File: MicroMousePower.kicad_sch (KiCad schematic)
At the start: 40 parts, among them J1 USB_C_Receptacle_PowerOnly_6P, J2 Conn_02x16_Odd_Even, J3 Conn_01x02_Pin, T1 TIP31C, U1 INA219AxDCN, U2 MCP73831-3-MC, U3 CH224K, U4 DRV8833PW, U5 DRV8833PW, U6 TPS61023DRLR

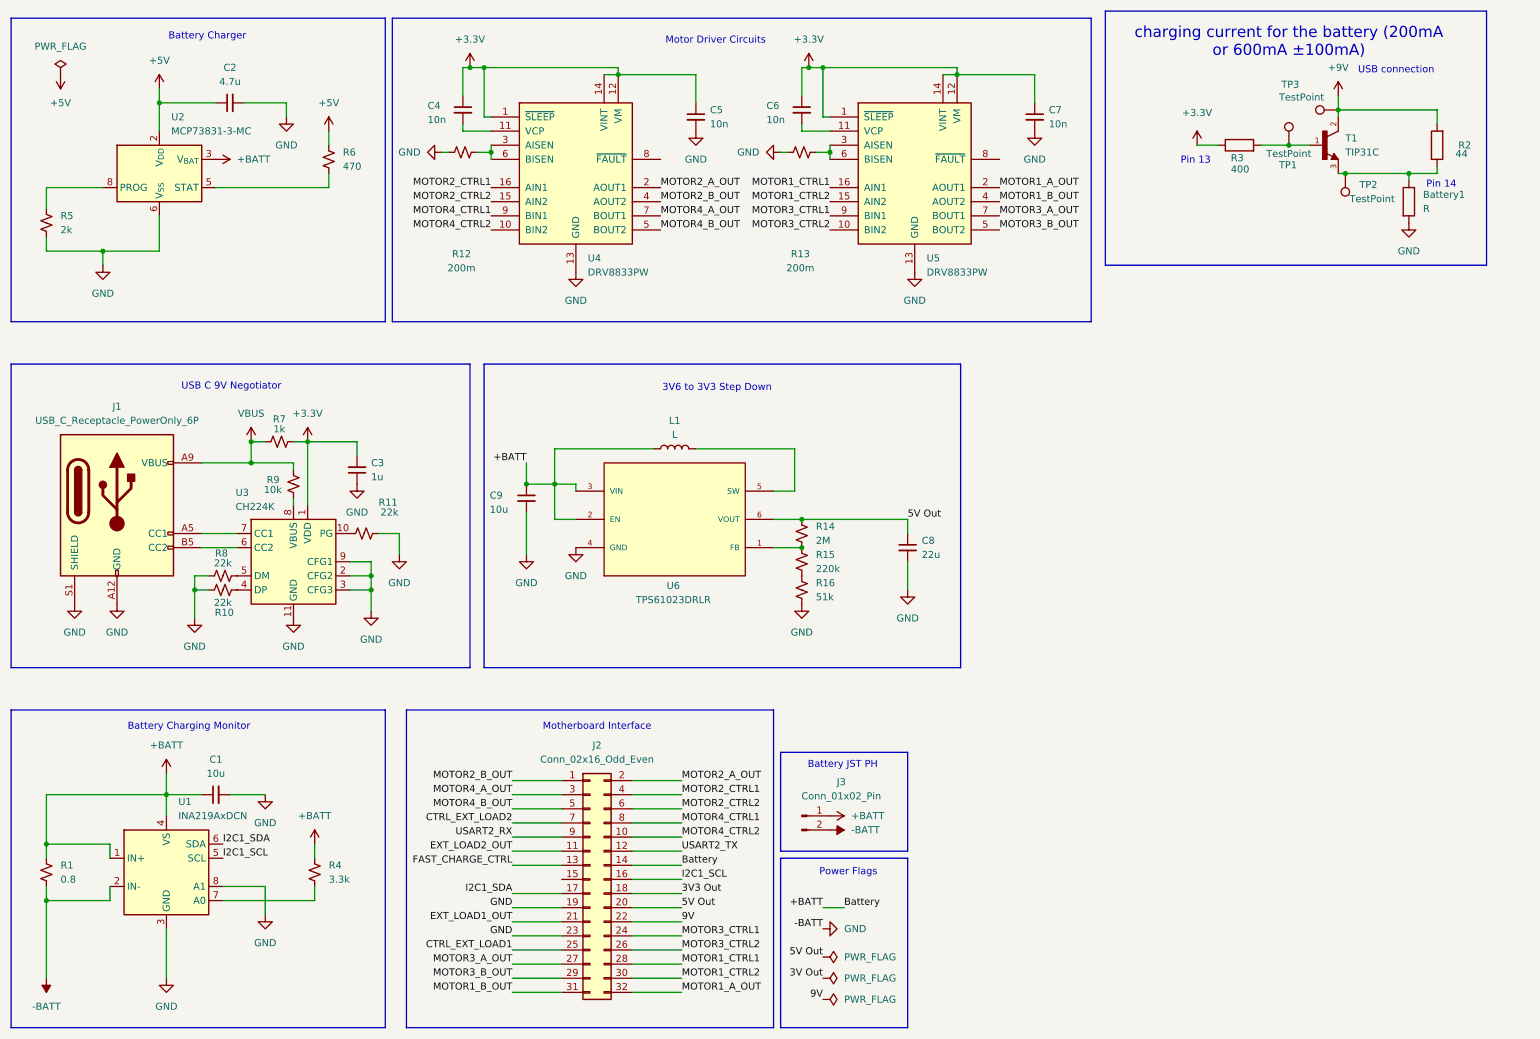
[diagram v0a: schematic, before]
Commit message: added current sources
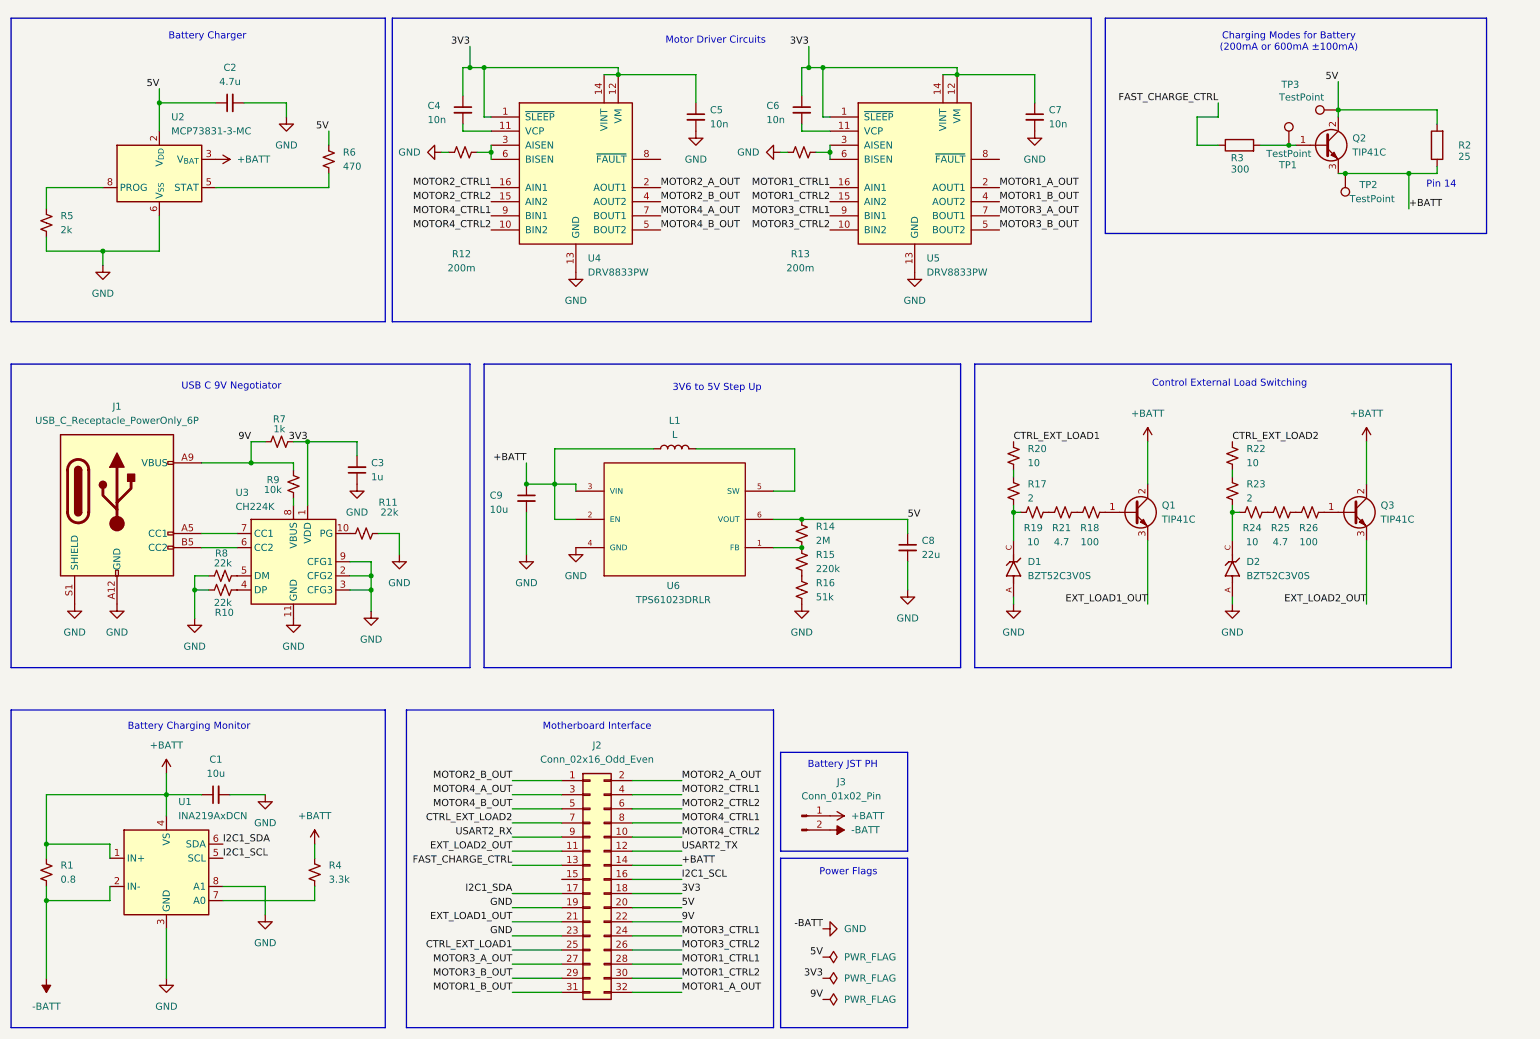
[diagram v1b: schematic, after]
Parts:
- removed Battery1: R, symbol Device:R
- removed T1: TIP31C, symbol TIP31C:TIP31C
- added D1, D2: BZT52C3V0S, BZT52C3V0S:DIO_BZT52C3V0S, symbol BZT52C3V0S:BZT52C3V0S
- added Q1, Q2, Q3: TIP41C, Package_TO_SOT_THT:TO-220-3_Vertical, symbol Transistor_BJT:TIP41C
- added R17, R23: 2, symbol Device:R_Small_US
- added R18, R26: 100, symbol Device:R_Small_US
- added R19, R20, R22, R24: 10, symbol Device:R_Small_US
- added R21, R25: 4.7, symbol Device:R_Small_US
- R2: value 44 -> 25
- R3: value 400 -> 300
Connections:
- net +9V is gone; now on net 5V: R2.2, TP3.1
- net 3V3 Out is gone; now on net 3V3: J2.18 (Pin_18)
- net 5V Out is gone; now on net 5V: C8.1, J2.20 (Pin_20), R14.1, U6.6 (VOUT)
- net VBUS is gone; now on net 9V: J1.A9 (VBUS), J1.B9 (VBUS), R7.1, R9.1
- net +BATT: now also R2.1, TP2.1, Q1.2 (C), Q2.3 (E), Q3.2 (C)
- net -BATT: now also D1.A, D2.A
- net CTRL_EXT_LOAD1: now also R20.1
- net CTRL_EXT_LOAD2: now also R22.1
- net EXT_LOAD1_OUT: now also Q1.3 (E)
- net EXT_LOAD2_OUT: now also Q3.3 (E)
- net FAST_CHARGE_CTRL: now also R3.1
- net at R3.2, TP1.1: now also Q2.1 (B)
- net +3.3V renamed 3V3
- net 3V3: no longer R3.1
- net +5V renamed 5V
- net 5V: now also Q2.2 (C)
- new net: R22.2, R23.1
- new net: D2.C, R23.2, R24.1
- new net: R19.2, R21.1
- new net: R18.1, R21.2
- new net: Q3.1 (B), R26.2
- new net: Q1.1 (B), R18.2
- new net: R25.2, R26.1
- new net: R24.2, R25.1
- new net: D1.C, R17.2, R19.1
- new net: R17.1, R20.2
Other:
- note added: "3V6 to 5V Step Up"
- note added: "Charging Modes for Battery (200mA or 600mA ±100mA)"
- note added: "Control External Load Switching"
- note removed: "3V6 to 3V3 Step Down"
- note removed: "Pin 13"
- note removed: "USB connection"
- note removed: "charging current for the battery (200mA or 600mA ±100mA)"

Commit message: added LCSC values to all components
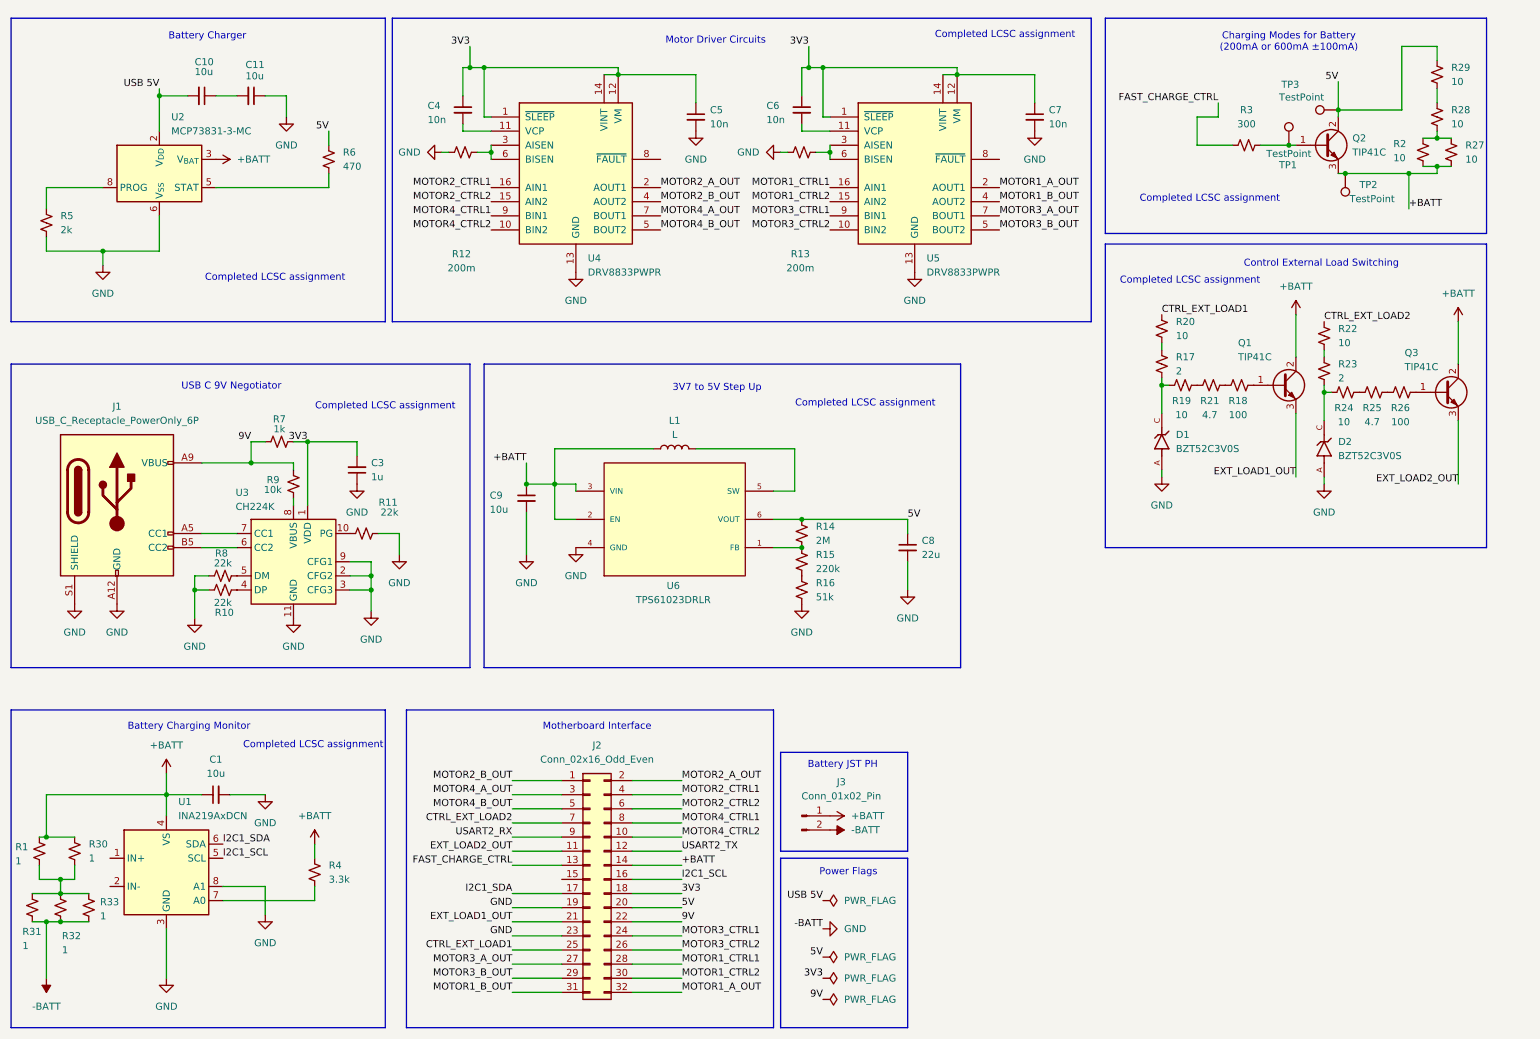
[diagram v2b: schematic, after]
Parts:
- removed C2: 4.7u, symbol Device:C_Small
- removed R2: 25, symbol Device:R
- removed R3: 300, symbol Device:R
- added C10, C11: 10u, symbol Device:C_Small
- added R2, R27, R28, R29: 10, symbol Device:R_Small_US
- added R3: 300, symbol Device:R_Small_US
- added R30, R31, R32, R33: 1, symbol Device:R_Small_US
- C1, C9: LCSC (none) -> C15850
- C3: LCSC (none) -> C52923
- C4, C5, C6, C7: LCSC (none) -> C15195
- C8: LCSC (none) -> C12891
- D1, D2: LCSC (none) -> C19077436
- J1: LCSC (none) -> C168701
- Q1, Q3: LCSC (none) -> C92603
- R1: value 0.8 -> 1; LCSC (none) -> C22936
- R10, R8: LCSC (none) -> C17560
- R11: LCSCf (none) -> C17560
- R14: LCSC (none) -> C22976
- R15: LCSC (none) -> C17556
- R16: LCSC (none) -> C17737
- R17, R23: LCSC (none) -> C22977
- R18, R26: LCSC (none) -> C17901
- R19, R20, R22, R24, R25: LCSC (none) -> C17903
- R21: LCSC (none) -> C23164
- R4: LCSC (none) -> C26010
- R5: LCSC (none) -> C17604
- R6: LCSC (none) -> C17710
- R7: LCSC (none) -> C4410
- R9: LCSC (none) -> C17902
- U1: LCSC (none) -> 87469
- U2: LCSC (none) -> C635038
- U3: LCSC (none) -> C970725
- U4, U5: value DRV8833PW -> DRV8833PWPR; LCSC (none) -> C50506
- U6: LCSC (none) -> C919459
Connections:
- net +BATT: now also R2.2, R27.2, R30.1; no longer U1.1 (IN+)
- net -BATT: now also C11.1, R31.2, R32.2, R33.2; no longer R1.2, U1.2 (IN-)
- net 5V: now also R29.1; no longer U2.1 (V_{DD}), U2.2 (V_{DD})
- net FAST_CHARGE_CTRL: now also R3.1
- net at Q2.1 (B), TP1.1: now also R3.2
- new net: R28.1, R29.2
- new net: R2.1, R27.1, R28.2
- new net: R1.2, R30.2, R31.1, R32.1, R33.1
- new net: C10.1, C11.2
- new net USB 5V: C10.2, U2.1 (V_{DD}), U2.2 (V_{DD})
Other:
- note added: "3V7 to 5V Step Up"
- note added: "Completed LCSC assignment"
- note removed: "3V6 to 5V Step Up"
- note removed: "Pin 14"
- moved on the sheet: D1, D2, Q1, Q3, R17, R18, R19, R20, R21, R22, R23, R24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

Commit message: completed schematic with LCSC codes
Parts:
- added C12, C13: 10u, symbol Device:C_Small
- added C14, C2: 4.7u, symbol Device:C_Small
- added L2, L3, L4, L5: 2.2u, symbol Device:L
- added R34: 51k, symbol Device:R_Small_US
- added R35: 1.2k, symbol Device:R_Small_US
- added R36: 10k, symbol Device:R_Small_US
- added U7: TPS62743YFPT, TPS62743YFPT:BGA8N40P2X4_87X156X50, symbol TPS62743YFPT:TPS62743YFPT
- added U8: AP62300WU, Package_TO_SOT_SMD:TSOT-23-6, symbol Regulator_Switching:AP62300WU
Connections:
- net +BATT: now also C2.2, U7.B1 (EN), U7.C1 (VSEL1), U7.C2 (VOS), U7.D1 (VSEL2), U7.D2 (VSEL3)
- net -BATT: now also C12.2, C13.2, C2.1, R36.1, U7.B2 (GND), U8.1 (GND)
- net 3V3: now also C12.1, L2.2, U7.A1 (SW)
- net 5V: now also L5.2, R34.1
- net 9V: now also C13.1, U8.3 (IN)
- new net: R34.2, R35.1
- new net: L2.1, U7.A2 (VIN)
- new net: C14.1, L3.1, L4.1, U8.2 (SW)
- new net: L3.2, L4.2, L5.1
- new net: R35.2, R36.2
- new net: C14.2, U8.6 (BST)
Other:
- note added: "3V7 to 3V3"
- note added: "9V to 5V"

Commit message: fixed ERC errors
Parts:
- added C15: 22u, symbol Device:C_Small
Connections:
- net +BATT: now also C1.2, C11.1, C12.2, C13.2, C2.1, C3.1, C5.2, C7.2, C9.2, D1.A, D2.A, J1.A12 (GND), J1.B12 (GND), J1.S1 (SHIELD), J2.19 (Pin_19), J2.23 (Pin_23), J3.2 (Pin_2), L2.1, R10.2, R11.2, R12.1, R13.1, R16.2, R31.2, R32.2, R33.2, R36.1, R5.2, R8.1, U1.1 (IN+), U1.3 (GND), U1.8 (A1), U2.6 (V_{SS}), U3.11 (GND), U3.2 (CFG2), U3.3 (CFG3), U3.9 (CFG1), U4.13 (GND), U5.13 (GND), U6.4 (GND), U7.A1 (SW), U7.A2 (VIN), U7.B2 (GND), U8.1 (GND), C15.2
- net 3V3: no longer U7.A1 (SW)
- net 5V: no longer L5.2, R34.1
- net 9V: now also U8.5 (EN)
- net USB 5V: now also L5.2, R34.1
- net at R35.2, R36.2: now also U8.4 (FB)
- net at R1.2, R30.2, R31.1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: now also U1.2 (IN-)
- removed net -BATT: C1.2, C11.1, C12.2, C13.2, C2.1, C3.1, C5.2, C7.2, C8.2, C9.2, D1.A, D2.A, J1.A12 (GND), J1.B12 (GND), J1.S1 (SHIELD), J2.19 (Pin_19), J2.23 (Pin_23), J3.2 (Pin_2), R10.2, R11.2, R12.1, R13.1, R16.2, R31.2, R32.2, R33.2, R36.1, R5.2, R8.1, U1.3 (GND), U1.8 (A1), U2.6 (V_{SS}), U3.11 (GND), U3.2 (CFG2), U3.3 (CFG3), U3.9 (CFG1), U4.13 (GND), U5.13 (GND), U6.4 (GND), U7.B2 (GND), U8.1 (GND)
- new net: C15.1, C8.2
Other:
- moved on the sheet: C12, C13, C14, C2, L2, L3, L4, L5, R34, R35, R36, U7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

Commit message: fixed more ERC errors
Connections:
- net +BATT: no longer C1.2, C11.1, C12.2, C13.2, C15.2, C2.1, C3.1, C5.2, C7.2, C9.2, D1.A, D2.A, J1.A12 (GND), J1.B12 (GND), J1.S1 (SHIELD), J2.19 (Pin_19), J2.23 (Pin_23), J3.2 (Pin_2), L2.1, R10.2, R11.2, R12.1, R13.1, R16.2, R31.2, R32.2, R33.2, R36.1, R5.2, R8.1, U1.3 (GND), U1.8 (A1), U2.6 (V_{SS}), U3.11 (GND), U3.2 (CFG2), U3.3 (CFG3), U3.9 (CFG1), U4.13 (GND), U5.13 (GND), U6.4 (GND), U7.A1 (SW), U7.B2 (GND), U7.C2 (VOS), U8.1 (GND)
- new net: L2.1, U7.A1 (SW), U7.C2 (VOS)
- new net -BATT: C1.2, C11.1, C12.2, C13.2, C15.2, C2.1, C3.1, C5.2, C7.2, C9.2, D1.A, D2.A, J1.A12 (GND), J1.B12 (GND), J1.S1 (SHIELD), J2.19 (Pin_19), J2.23 (Pin_23), J3.2 (Pin_2), R10.2, R11.2, R12.1, R13.1, R16.2, R31.2, R32.2, R33.2, R36.1, R5.2, R8.1, U1.3 (GND), U1.8 (A1), U2.6 (V_{SS}), U3.11 (GND), U3.2 (CFG2), U3.3 (CFG3), U3.9 (CFG1), U4.13 (GND), U5.13 (GND), U6.4 (GND), U7.B2 (GND), U8.1 (GND)
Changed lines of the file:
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@@
 	)
 	(junction
-		(at 265.43 127)
-		(diameter 0)
-		(color 0 0 0 0)
-	)
-	(junction
 		(at 265.43 41.91)
 		(diameter 0)
@@
 	)
 	(junction
-		(at 265.43 121.92)
-		(diameter 0)
-		(color 0 0 0 0)
-	)
-	(junction
 		(at 22.86 170.18)
 		(diameter 0)
@@
 	(wire
 		(pts
-			(xy 265.43 130.81) (xy 222.25 130.81)
-		)
-		(stroke
-			(width 0)
-			(type default)
-		)
-	)
-	(wire
-		(pts
 			(xy 276.86 143.51) (xy 276.86 146.05)
 		)
@@
 	(wire
 		(pts
-			(xy 265.43 121.92) (xy 265.43 127)
-		)
-		(stroke
-			(width 0)
-			(type default)
-		)
-	)
-	(wire
-		(pts
 			(xy 115.57 97.79) (xy 115.57 99.06)
 		)
@@
 	(wire
 		(pts
+			(xy 261.62 130.81) (xy 222.25 130.81)
+		)
+		(stroke
+			(width 0)
+			(type default)
+		)
+	)
+	(wire
+		(pts
 			(xy 265.43 121.92) (xy 267.97 121.92)
 		)
@@
 	(wire
 		(pts
-			(xy 265.43 116.84) (xy 265.43 121.92)
-		)
-		(stroke
-			(width 0)
-			(type default)
-		)
-	)
-	(wire
-		(pts
 			(xy 220.98 78.74) (xy 220.98 80.01)
 		)
@@
 	(wire
 		(pts
+			(xy 265.43 127) (xy 269.24 127)
+		)
+		(stroke
+			(width 0)
+			(type default)
+		)
+	)
+	(wire
+		(pts
 			(xy 151.13 104.14) (xy 156.21 104.14)
 		)
@@
 	(wire
 		(pts
-			(xy 48.26 93.98) (xy 57.15 93.98)
+			(xy 261.62 119.38) (xy 261.62 130.81)
 		)
 		(stroke
@@
 	(wire
 		(pts
-			(xy 259.08 147.32) (xy 261.62 147.32)
+			(xy 48.26 93.98) (xy 57.15 93.98)
 		)
 		(stroke
@@
 	(wire
 		(pts
-			(xy 265.43 127) (xy 265.43 130.81)
+			(xy 259.08 147.32) (xy 261.62 147.32)
 		)
 		(stroke
@@
 	(wire
 		(pts
+			(xy 265.43 119.38) (xy 261.62 119.38)
+		)
+		(stroke
+			(width 0)
+			(type default)
+		)
+	)
+	(wire
+		(pts
 			(xy 175.26 104.14) (xy 175.26 106.68)
 		)
@@
 	(wire
 		(pts
+			(xy 265.43 116.84) (xy 265.43 119.38)
+		)
+		(stroke
+			(width 0)
+			(type default)
+		)
+	)
+	(wire
+		(pts
 			(xy 245.11 67.31) (xy 245.11 74.93)
 		)
@@
 	)
 	(symbol
+		(lib_id "power:GND")
+		(at 20.32 186.69 0)
+		(unit 1)
+		(exclude_from_sim no)
+		(in_bom yes)
+		(on_board yes)
+		(dnp no)
+		(fields_autoplaced yes)
+		(property "Reference" "#PWR010"
+			(at 20.32 193.04 0)
+			(effects
+				(font
+					(size 1.27 1.27)
+				)
+				(hide yes)
+			)
+		)
+		(property "Value" "GND"
+			(at 20.32 191.77 0)
+			(effects
+				(font
+					(size 1.27 1.27)
+				)
+			)
+		)
+		(property "Footprint" ""
+			(at 20.32 186.69 0)
+			(effects
+				(font
+					(size 1.27 1.27)
+				)
+				(hide yes)
+			)
+		)
+		(property "Datasheet" ""
+			(at 20.32 186.69 0)
+			(effects
+				(font
+					(size 1.27 1.27)
+				)
+				(hide yes)
+			)
+		)
+		(property "Description" "Power symbol creates a global label with name \"GND\" , ground"
+			(at 20.32 186.69 0)
+			(effects
+				(font
+					(size 1.27 1.27)
+				)
+				(hide yes)
+			)
+		)
+		(pin "1"
+		)
+		(instances
+			(project "MicroMousePower"
+				(path "/eac97a68-d510-4c4f-b246-1e946de69ee0"
+					(reference "#PWR010")
+					(unit 1)
+				)
+			)
+		)
+	)
+	(symbol
 		(lib_id "Device:R_Small_US")
 		(at 276.86 148.59 0)
@@
 	(symbol
 		(lib_id "power:GND")
-		(at 265.43 127 90)
+		(at 269.24 127 90)
 		(unit 1)
 		(exclude_from_sim no)
@@
 		(fields_autoplaced yes)
 		(property "Reference" "#PWR014"
-			(at 271.78 127 0)
+			(at 275.59 127 0)
 			(effects
 				(font
@@
 		)
 		(property "Value" "GND"
-			(at 269.24 126.9999 90)
+			(at 273.05 126.9999 90)
 			(effects
 				(font
@@
 		)
 		(property "Footprint" ""
-			(at 265.43 127 0)
+			(at 269.24 127 0)
 			(effects
 				(font
@@
 		)
 		(property "Datasheet" ""
-			(at 265.43 127 0)
+			(at 269.24 127 0)
 			(effects
 				(font
@@
 		)
 		(property "Description" "Power symbol creates a global label with name \"GND\" , ground"
-			(at 265.43 127 0)
+			(at 269.24 127 0)
 			(effects
 				(font
@@
 					(unit 1)
 				)
-			)
-		)
-	)
-	(symbol
-		(lib_id "power:-BATT")
-		(at 20.32 186.69 180)
-		(unit 1)
-		(exclude_from_sim no)
-		(in_bom yes)
-		(on_board yes)
-		(dnp no)
-		(fields_autoplaced yes)
-		(property "Reference" "#PWR010"
-			(at 20.32 182.88 0)
-			(effects
-				(font
-					(size 1.27 1.27)
-				)
-				(hide yes)
-			)
-		)
-		(property "Value" "-BATT"
-			(at 20.32 191.77 0)
-			(effects
-				(font
-					(size 1.27 1.27)
-				)
-			)
-		)
-		(property "Footprint" ""
-			(at 20.32 186.69 0)
-			(effects
-				(font
-					(size 1.27 1.27)
-				)
-				(hide yes)
-			)
-		)
-		(property "Datasheet" ""
-			(at 20.32 186.69 0)
-			(effects
-				(font
-					(size 1.27 1.27)
-				)
-				(hide yes)
-			)
-		)
-		(property "Description" "Power symbol creates a global label with name \"-BATT\""
-			(at 20.32 186.69 0)
-			(effects
-				(font
-					(size 1.27 1.27)
-				)
-				(hide yes)
-			)
-		)
-		(pin "1"
-		)
-		(instances
-			(project ""
-				(path "/eac97a68-d510-4c4f-b246-1e946de69ee0"
-					(reference "#PWR010")
-					(unit 1)
-				)

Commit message: meow idk?
pss pss
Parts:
- added R37, R38: 10k, symbol Device:R_Small_US
- added TP10, TP11, TP12, TP13, TP14, TP15, TP16, TP4, TP5, TP6, TP7, TP8, TP9: TestPoint, symbol Connector:TestPoint
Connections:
- net +BATT: now also TP10.1, TP14.1, TP16.1, TP4.1
- net -BATT: now also R38.1
- net 5V: now also TP15.1
- net 9V: now also R37.2; no longer U8.5 (EN)
- net EXT_LOAD1_OUT: now also TP13.1
- net EXT_LOAD2_OUT: now also TP12.1
- net USB 5V: now also TP8.1
- net at L2.1, U7.A1 (SW), U7.C2 (VOS): now also TP6.1, TP7.1
- net at D2.C, R23.2, R24.1: now also TP11.1
- net at D1.C, R17.2, R19.1: now also TP5.1
- new net: R37.1, R38.2, TP9.1, U8.5 (EN)
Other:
- moved on the sheet: C13, U8
